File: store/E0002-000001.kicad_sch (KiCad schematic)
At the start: 11 parts, among them J1 Power_IN, J2 Connector, J5 Seansor_Header_A, J6 Seansor_Header_B, U1 INA226

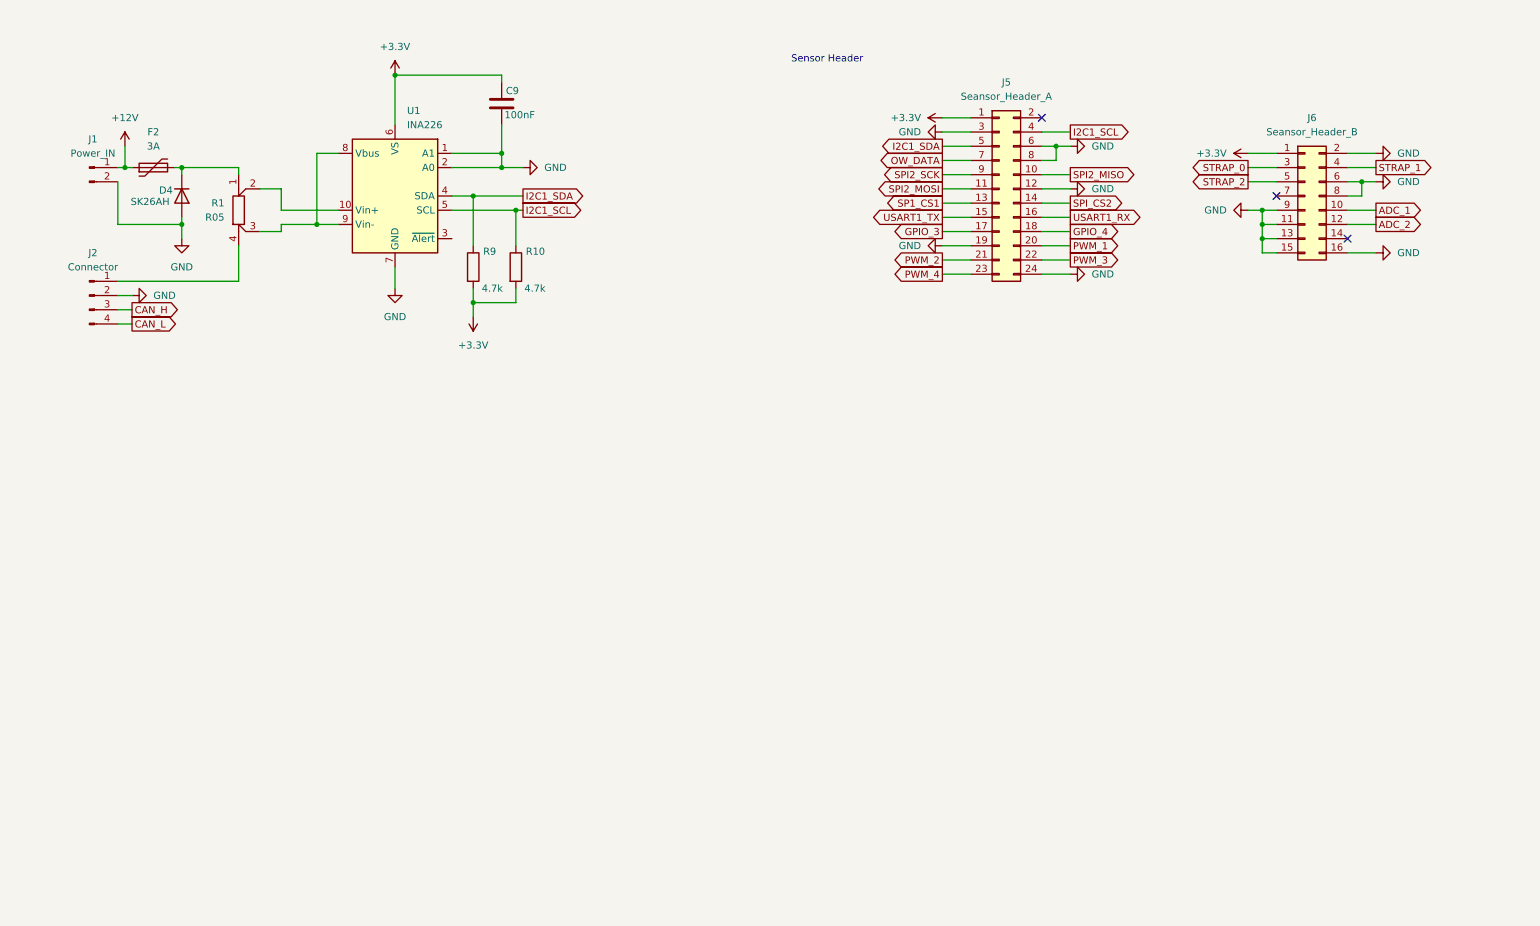
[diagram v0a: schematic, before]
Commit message: docs(adr): M05 sense-only; over-temp trip moves to heating actuator
Refine the M05-SAFETY model across ADR-0014/0015/0018: M05 is sense-only
(TMP117 reports cabinet air, single INA226 on the +12 V bus, reed/leak
report-alert only). The hardware-independent over-temperature trip moves
off M05 to the heating-actuator node (thermistor/PT1000 + comparator ->
relay-enable) per the sense/switch separation. Leak/door are report/alert
only with software-mediated response over Cyphal.

Update E0002 schematic to the sense-only complement (TMP117 + INA226,
gated leak-electrode excitation) and reconcile stale downstream refs in
REGISTRY.md and README.md.

Signed-off-by: IIchukissII <133657307+IIchukissII@users.noreply.github.com>
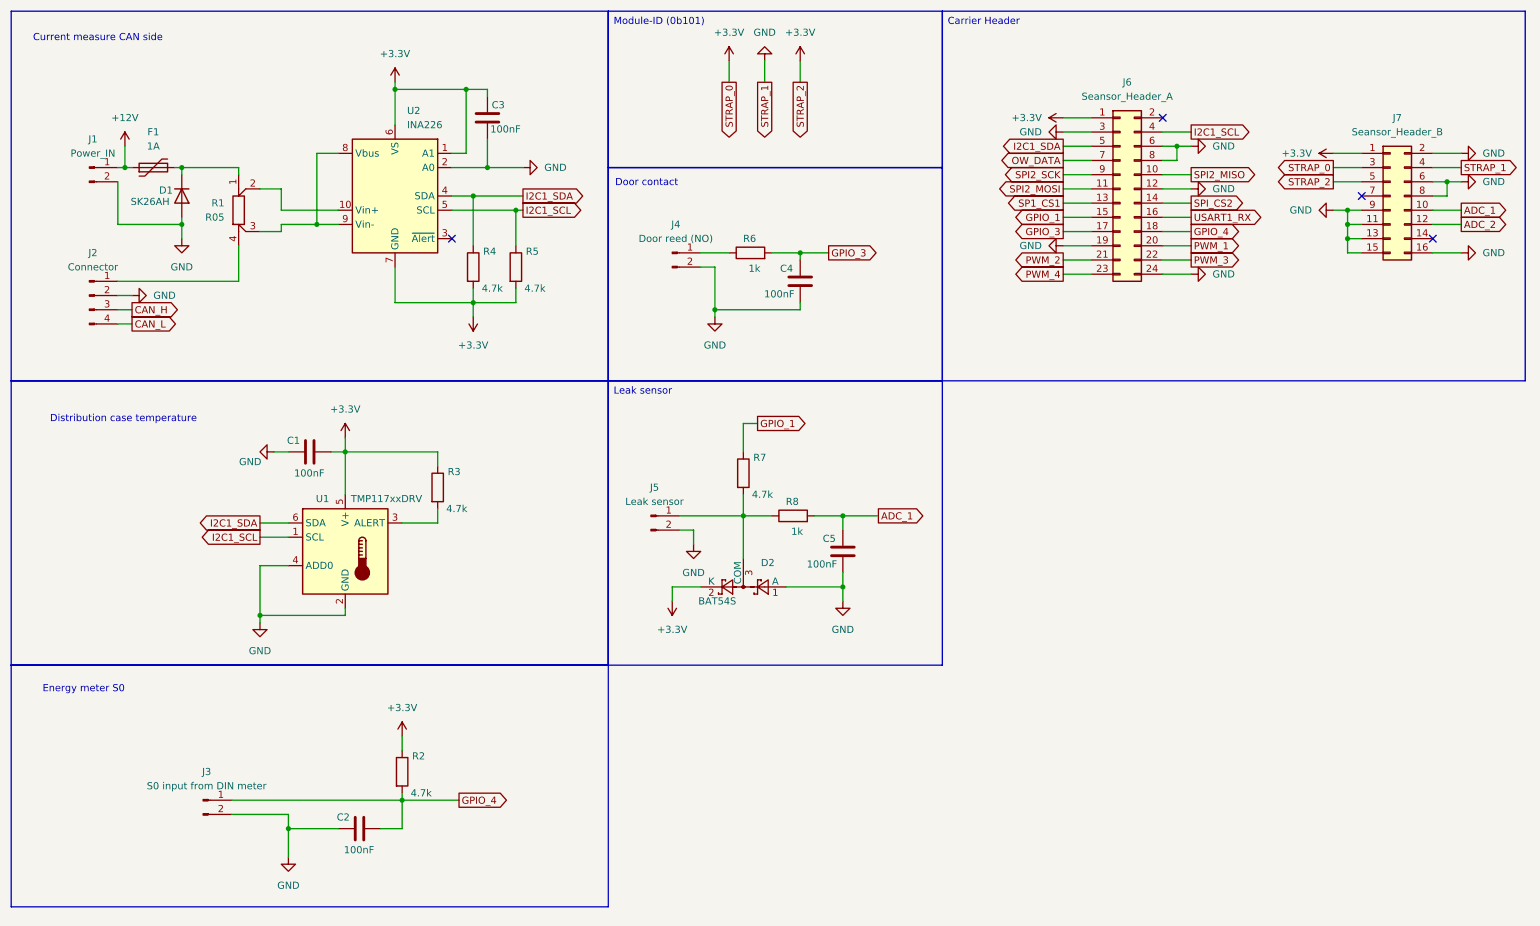
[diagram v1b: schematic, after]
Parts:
- added C1, C2, C4, C5: 100nF, Capacitor_SMD:C_0805_2012Metric, symbol Device:C
- added D2: BAT54S, Package_TO_SOT_SMD:SOT-23, symbol Diode:BAT54S
- added J3: S0 input from DIN meter, Connector_Phoenix_SPT:PhoenixContact_SPT_2.5_2-H-5.0_1x02_P5.0mm_Horizontal, symbol Connector:Conn_01x02_Pin
- added J4: Door reed (NO), Connector_Phoenix_SPT:PhoenixContact_SPT_2.5_2-H-5.0_1x02_P5.0mm_Horizontal, symbol Connector:Conn_01x02_Pin
- added J5: Leak sensor, Connector_Phoenix_SPT:PhoenixContact_SPT_2.5_2-H-5.0_1x02_P5.0mm_Horizontal, symbol Connector:Conn_01x02_Pin
- added R2, R3, R7: 4.7k, Resistor_SMD:R_0805_2012Metric, symbol Device:R
- added R6, R8: 1k, Resistor_SMD:R_0805_2012Metric, symbol Device:R
- added U1: TMP117xxDRV, Package_SON:WSON-6-1EP_2x2mm_P0.65mm_EP1x1.6mm, symbol Sensor_Temperature:TMP117xxDRV
- F1: renamed from F2; value 3A -> 1A
- J1: footprint (none) -> Connector_Phoenix_SPT:PhoenixContact_SPT_2.5_2-H-5.0_1x02_P5.0mm_Horizontal
- renumbered C9 to C3, D4 to D1, J5 to J6, J6 to J7, R9 to R4, R10 to R5, U1 to U2
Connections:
- net STRAP_0 is gone; now on net +3.3V: J7.3 (Pin_3)
- net STRAP_1 is gone; now on net GND: J7.4 (Pin_4)
- net STRAP_2 is gone; now on net +3.3V: J7.5 (Pin_5)
- net +3.3V: now also U2.1 (A1), U2.7 (GND), C1.1, D2.2 (K), R2.1, R3.1, U1.5 (V+)
- net ADC_1: now also C5.2, R8.2
- net GND: now also C1.2, C2.2, C4.1, C5.1, D2.1 (A), J3.2 (Pin_2), J4.2 (Pin_2), J5.2 (Pin_2), U1.2 (GND), U1.4 (ADD0); no longer U2.1 (A1), U2.7 (GND)
- net GPIO_3: now also C4.2, R6.2
- net GPIO_4: now also C2.1, J3.1 (Pin_1), R2.2
- net I2C1_SCL: now also U1.1 (SCL)
- net I2C1_SDA: now also U1.6 (SDA)
- net USART1_TX renamed GPIO_1
- net GPIO_1: now also R7.1
- new net: R3.2, U1.3 (ALERT)
- new net: J4.1 (Pin_1), R6.1
- new net: D2.3 (COM), J5.1 (Pin_1), R7.2, R8.1
- no-connect marks 3 -> 4
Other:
- note added: "Current measure CAN side"
- note added: "Distribution case temperature"
- note added: "Door contact"
- note added: "Energy meter S0"
- note removed: "Sensor Header"
- moved on the sheet: C3, J6, J7

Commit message: feat(E0002): update schematic and begin PCB layout
Revise the E0002-000001 schematic and start the corresponding PCB layout, with associated project/prl settings updates.

Signed-off-by: IIchukissII <133657307+IIchukissII@users.noreply.github.com>
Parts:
- removed R1: R05, symbol PCM_Resistor_AKL:R_Shunt_Generic
- added D6: 12V, LED_SMD:LED_0805_2012Metric, symbol Device:LED
- added R1: 0R1, PCM_Resistor_SMD_AKL:R_2512_6332Metric, symbol Device:R
- added R11: 4.7k, Resistor_SMD:R_0805_2012Metric, symbol Device:R
- J1, J3: footprint Connector_Phoenix_SPT:PhoenixContact_SPT_2.5_2-H-5.0_1x02_P5.0mm_Horizontal -> TerminalBlock_Phoenix:TerminalBlock_Phoenix_MKDS-1,5-2_1x02_P5.00mm_Horizontal
- J4: renamed from J5; footprint Connector_Phoenix_SPT:PhoenixContact_SPT_2.5_2-H-5.0_1x02_P5.0mm_Horizontal -> TerminalBlock_Phoenix:TerminalBlock_Phoenix_MKDS-1,5-2_1x02_P5.00mm_Horizontal
- J5: renamed from J4; footprint Connector_Phoenix_SPT:PhoenixContact_SPT_2.5_2-H-5.0_1x02_P5.0mm_Horizontal -> TerminalBlock_Phoenix:TerminalBlock_Phoenix_MKDS-1,5-2_1x02_P5.00mm_Horizontal
- J6: footprint Connector_PinSocket_2.54mm:PinSocket_2x12_P2.54mm_Vertical_SMD -> Connector_PinHeader_2.54mm:PinHeader_2x12_P2.54mm_Vertical
- J7: footprint Connector_PinSocket_2.54mm:PinSocket_2x08_P2.54mm_Vertical_SMD -> Connector_PinHeader_2.54mm:PinHeader_2x08_P2.54mm_Vertical
- renumbered R7 to R6, R6 to R7
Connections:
- net +12V: now also R11.1
- net GND: now also D6.1 (K)
- net at D1.1 (K), F1.2: now also U2.10 (Vin+), R1.1
- net at J2.1 (Pin_1): now also U2.8 (Vbus), U2.9 (Vin-), R1.2
- new net: D6.2 (A), R11.2
